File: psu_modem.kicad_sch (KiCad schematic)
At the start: 9 parts, among them U10 LM2596S-ADJ

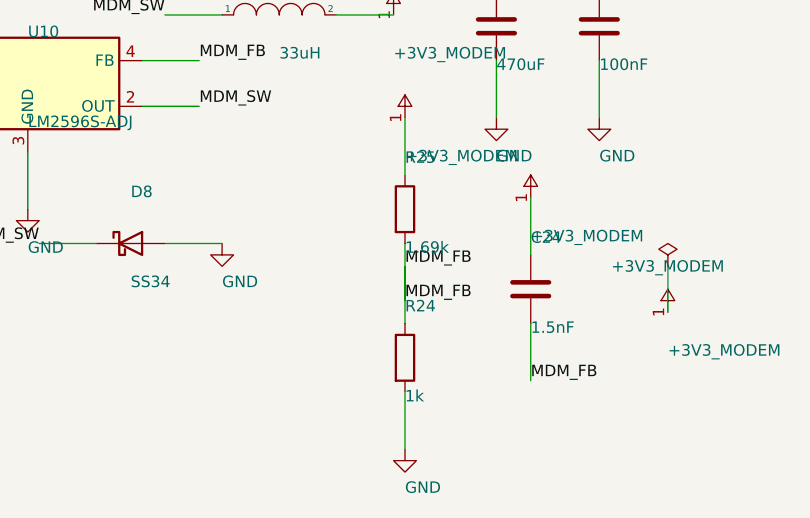
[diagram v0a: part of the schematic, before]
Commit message: WIP: J18/Q2/Q3/R30/R31 + reguardado KiCad de todas las hojas
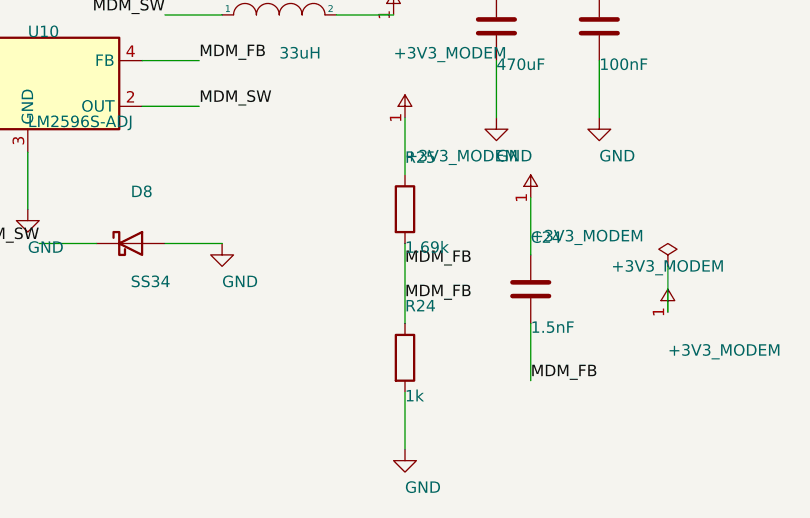
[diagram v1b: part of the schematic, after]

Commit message: friday changes
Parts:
- removed C24: 1.5nF, Capacitor_SMD:C_0805_2012Metric_Pad1.18x1.45mm_HandSolder, symbol Device:C
- removed D8: SS34, Diode_SMD:D_SMA, symbol Device:D_Schottky
- removed L2: 33uH, Inductor_SMD:L_Bourns_SDR1806, symbol pspice:INDUCTOR
- removed R24: 1k, Resistor_SMD:R_1206_3216Metric_Pad1.30x1.75mm_HandSolder, symbol Device:R
- removed R25: 1.69k, Resistor_SMD:R_1206_3216Metric_Pad1.30x1.75mm_HandSolder, symbol Device:R
- removed U10: LM2596S-ADJ, Package_TO_SOT_SMD:TO-263-5_TabPin3, symbol Regulator_Switching:LM2596S-ADJ
- added C33, C34: 4.7uF, Capacitor_SMD:C_1210_3225Metric, symbol Device:C
- added C35: 47nF, Capacitor_SMD:C_0805_2012Metric, symbol Device:C
- added C36, C37, C38: 47uF, Capacitor_SMD:C_1210_3225Metric, symbol Device:C
- added C39: 47pF, Capacitor_SMD:C_0402_1005Metric, symbol Device:C
- added C40: 0.47uF, Capacitor_SMD:C_0603_1608Metric, symbol Device:C
- added C41: 2.2uF, Capacitor_SMD:C_0603_1608Metric, symbol Device:C
- added C42: 1uF, Capacitor_SMD:C_0603_1608Metric, symbol Device:C
- added C43: 22nF, Capacitor_SMD:C_0402_1005Metric, symbol Device:C
- added L3: 10uH, Inductor_SMD:L_Bourns_SRR1260, symbol Device:L
- added R33: 1M, Resistor_SMD:R_0402_1005Metric, symbol Device:R
- added R34: 432k, Resistor_SMD:R_0402_1005Metric, symbol Device:R
- added R35: 78.7k, Resistor_SMD:R_0402_1005Metric, symbol Device:R
- added R36: 1.21M, Resistor_SMD:R_0402_1005Metric, symbol Device:R
- added R37, R38: 100k, Resistor_SMD:R_0402_1005Metric, symbol Device:R
- added U10: LM76003, Package_DFN_QFN:Texas_RNP0030B_WQFN-30-1EP_4x6mm_P0.5mm_EP1.8x4.5mm_ThermalVias, symbol Regulator_Switching:LM76003
- C25: value 100uF -> 47uF; footprint Capacitor_SMD:CP_Elec_8x10.5 -> Capacitor_SMD:CP_Elec_6.3x7.7; DigiKey (none) -> 4713-CV2-1H470MF80-RTR-ND; MPN (none) -> CV2-1H470MF80-R; Manufacturer (none) -> Cal-Chip Electronics, Inc.
- C26: DigiKey (none) -> 1189-2097-2-ND; MPN (none) -> 25TLV470M10X10.5; Manufacturer (none) -> Rubycon
- C27: DigiKey (none) -> 1276-1003-2-ND; MPN (none) -> CL21B104KBCNNNC; Manufacturer (none) -> Samsung Electro-Mechanics
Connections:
- net +24V: now also C33.1, C34.1, C35.1, R36.1, U10.20 (PVIN), U10.21 (PVIN), U10.22 (PVIN)
- net +3V3_MODEM: now also C36.1, C37.1, C38.1, C39.1, C42.1, L3.2, R33.1, R38.1, U10.9 (BIAS)
- net GND: now also C33.2, C34.2, C35.2, C36.2, C37.2, C38.2, C41.2, C42.2, C43.2, R34.2, R35.2, R37.2, U10.13 (AGND), U10.14 (AGND), U10.15 (AGND), U10.17 (SYNC/MODE), U10.19 (NC_{GND}), U10.24 (PGND), U10.25 (PGND), U10.26 (PGND), U10.27 (NC_{GND}), U10.28 (NC_{GND}), U10.29 (NC_{GND}), U10.30 (NC_{GND}), U10.31 (AGND)
- net MDM_FB: now also C39.2, R33.2, R34.1, U10.12 (FB)
- net MDM_SW: now also C40.2, L3.1, U10.1 (SW), U10.2 (SW), U10.3 (SW), U10.4 (SW), U10.5 (SW)
- new net MDM_BOOT: C40.1, U10.6 (BOOT)
- new net MDM_EN: R36.2, R37.1, U10.18 (EN)
- new net MDM_PG: R38.2, U10.16 (PGOOD)
- new net MDM_RT: R35.1, U10.10 (RT)
- new net MDM_SS: C43.1, U10.11 (SS/TRK)
- new net MDM_VCC: C41.1, U10.8 (VCC)
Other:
- title: PSU MODEM 3V3 - Convertidor reductor LM2596S-ADJ (+24V -> +3V3_MODEM) -> PSU MODEM 3V3 - Convertidor reductor sincrono LM76003 (+24V -> +3V3_MODEM)
- moved on the sheet: C25, C26, C27

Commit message: schematic updated
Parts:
- renumbered C40 to C19, C25 to C20, C41 to C21, C42 to C22, C39 to C23, C33 to C24, C34 to C25, C43 to C26, C35 to C27, C36 to C28, C37 to C29, C26 to C30, C38 to C31, C27 to C32, L3 to L2, R33 to R18, R34 to R19, R35 to R20, R36 to R21, R37 to R22, R38 to R23, U10 to U4

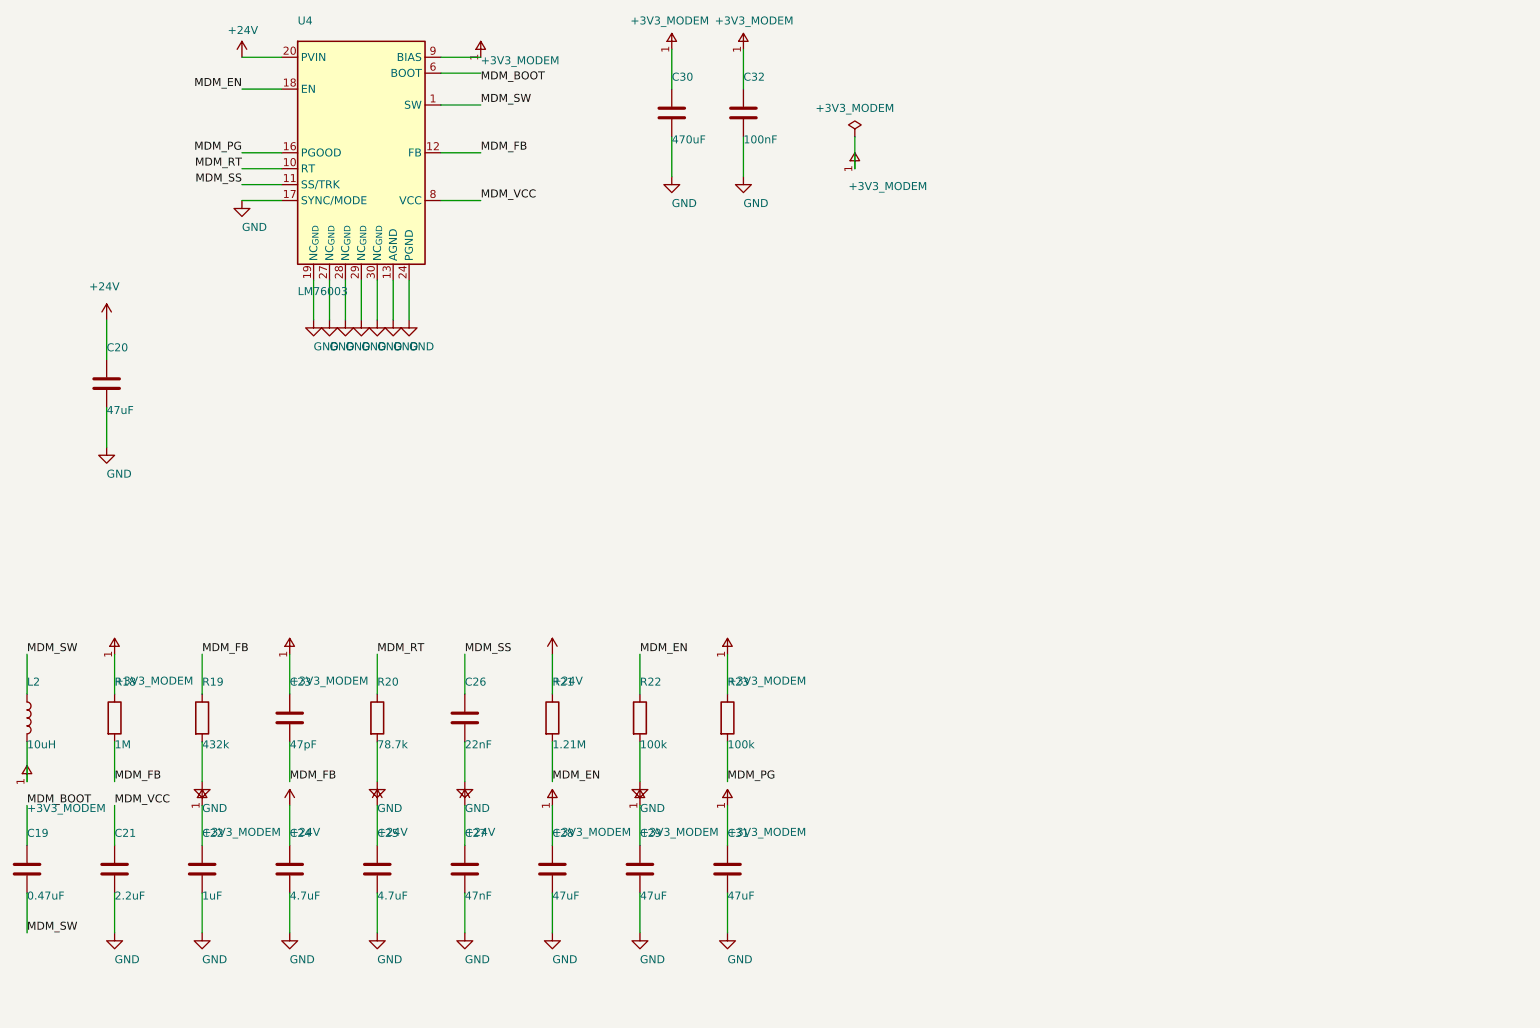
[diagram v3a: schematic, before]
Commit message: 2 power source
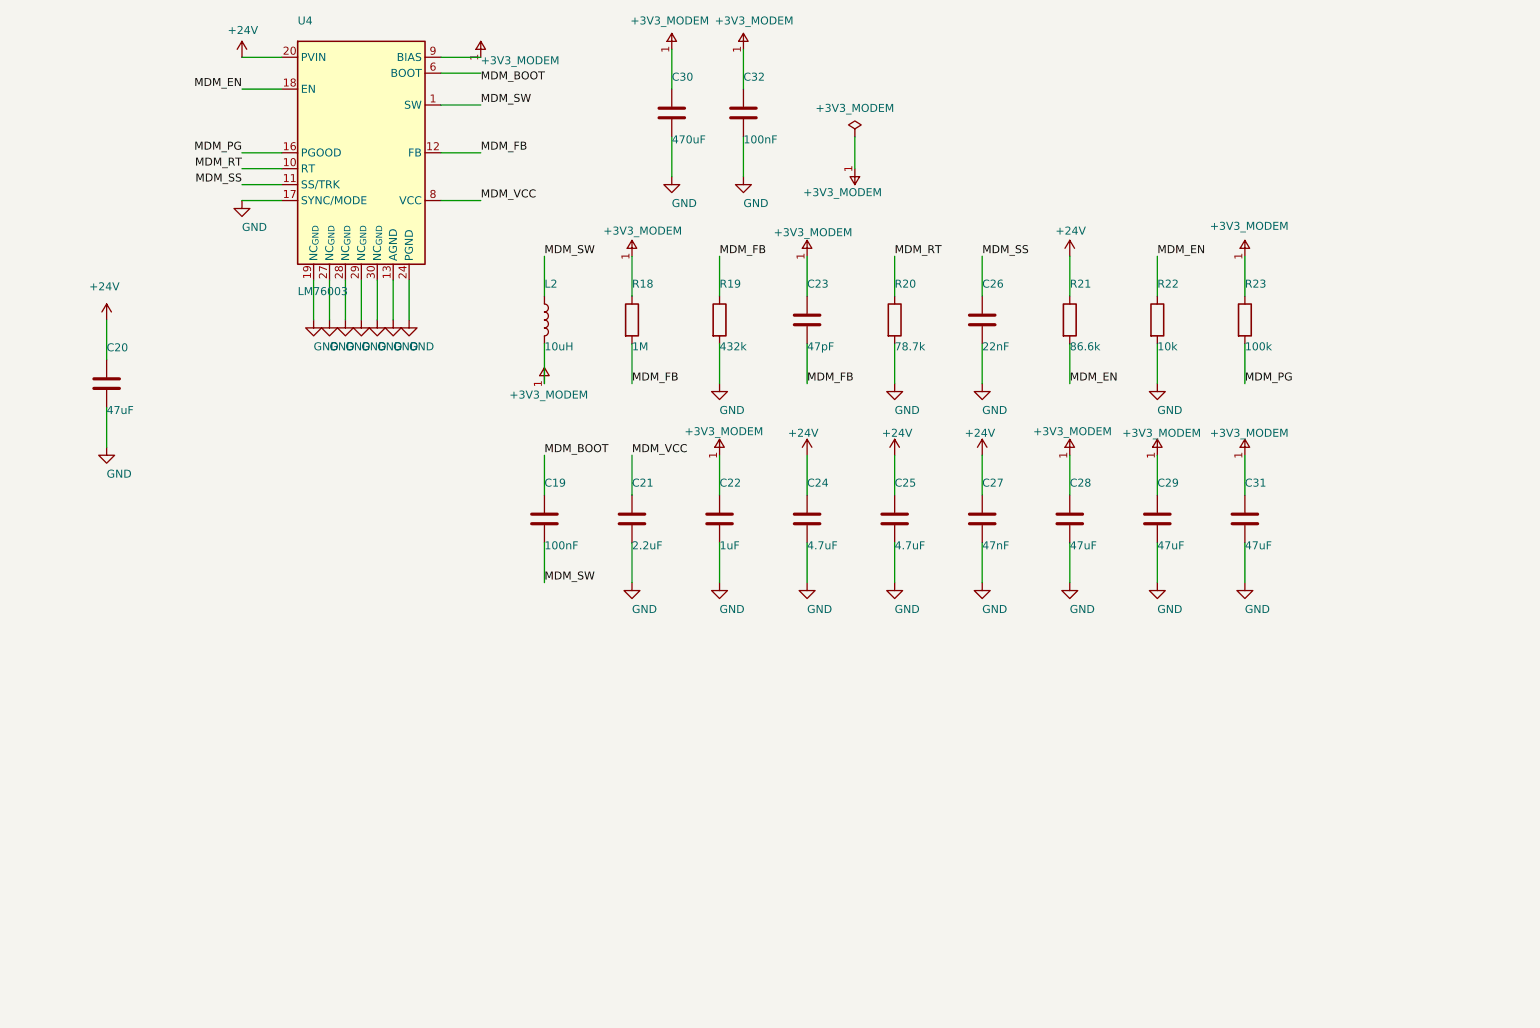
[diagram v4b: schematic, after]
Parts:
- C19: value 0.47uF -> 100nF; DigiKey 1276-2082-2-ND -> 1276-1000-1-ND; MPN CL10B474KA8NFNC -> CL10B104KB8NNNC
- R21: value 1.21M -> 86.6k; DigiKey RMCF0402FT1M21TR-ND -> RMCF0402FT86K6TR-ND; MPN RMCF0402FT1M21 -> RMCF0402FT86K6
- R22: value 100k -> 10k; DigiKey 311-100KLRTR-ND -> 311-10.0KLRTR-ND; MPN RC0402FR-07100KL -> RC0402FR-0710KL
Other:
- moved on the sheet: C19, C21, C22, C23, C24, C25, C26, C27, C28, C29, C31, L2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

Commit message: last changes in work
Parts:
- C19: value 100nF -> 470nF
- C31: value 47uF -> 56uF
- L2: value 10uH -> 4.7uH
- R18: value 1M -> 100k
- R19: value 432k -> 43.5k
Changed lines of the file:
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@@
 		)
 		(property "Value" "LM76003"
-			(at 80.01 67.31 0)
+			(at 86.614 24.13 0)
 			(effects
 				(font
@@
 			)
 		)
-		(property "Value" "10uH"
+		(property "Value" "4.7uH"
 			(at 119.38 76.12 0)
 			(effects
@@
 	(symbol
 		(lib_id "controlcarreta:+3V3_MODEM")
-		(at 119.38 81.28 0)
+		(at 119.38 81.28 180)
 		(unit 1)
 		(exclude_from_sim no)
@@
 		(dnp no)
 		(property "Reference" "#PWR061"
-			(at 119.38 76.28 0)
+			(at 119.38 86.28 0)
 			(effects
 				(font
@@
 		)
 		(property "Value" "+3V3_MODEM"
-			(at 113.792 83.82 0)
+			(at 125.73 84.582 0)
 			(effects
 				(font
@@
 			)
 		)
-		(property "Value" "1M"
+		(property "Value" "100k"
 			(at 133.35 76.12 0)
 			(effects
@@
 			)
 		)
-		(property "Value" "432k"
+		(property "Value" "43.5k"
 			(at 147.32 76.12 0)
 			(effects
@@
 			)
 		)
-		(property "Value" "100nF"
+		(property "Value" "470nF"
 			(at 119.38 107.87 0)
 			(effects
@@
 			)
 		)
-		(property "Value" "47uF"
+		(property "Value" "56uF"
 			(at 231.14 107.87 0)
 			(effects
